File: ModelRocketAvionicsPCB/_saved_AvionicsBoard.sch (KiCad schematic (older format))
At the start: 39 parts, among them CON1 microSD_Card, P1 FTSH-105-01-F-DV, P2 USB_OTG, P3 JST-2, SW1 SW_RST, U1 TM4C123GH6PM, U2 AT25SF161-16Mb_SPI_FLASH, Y1 16Mhz, Y2 32.768kHz

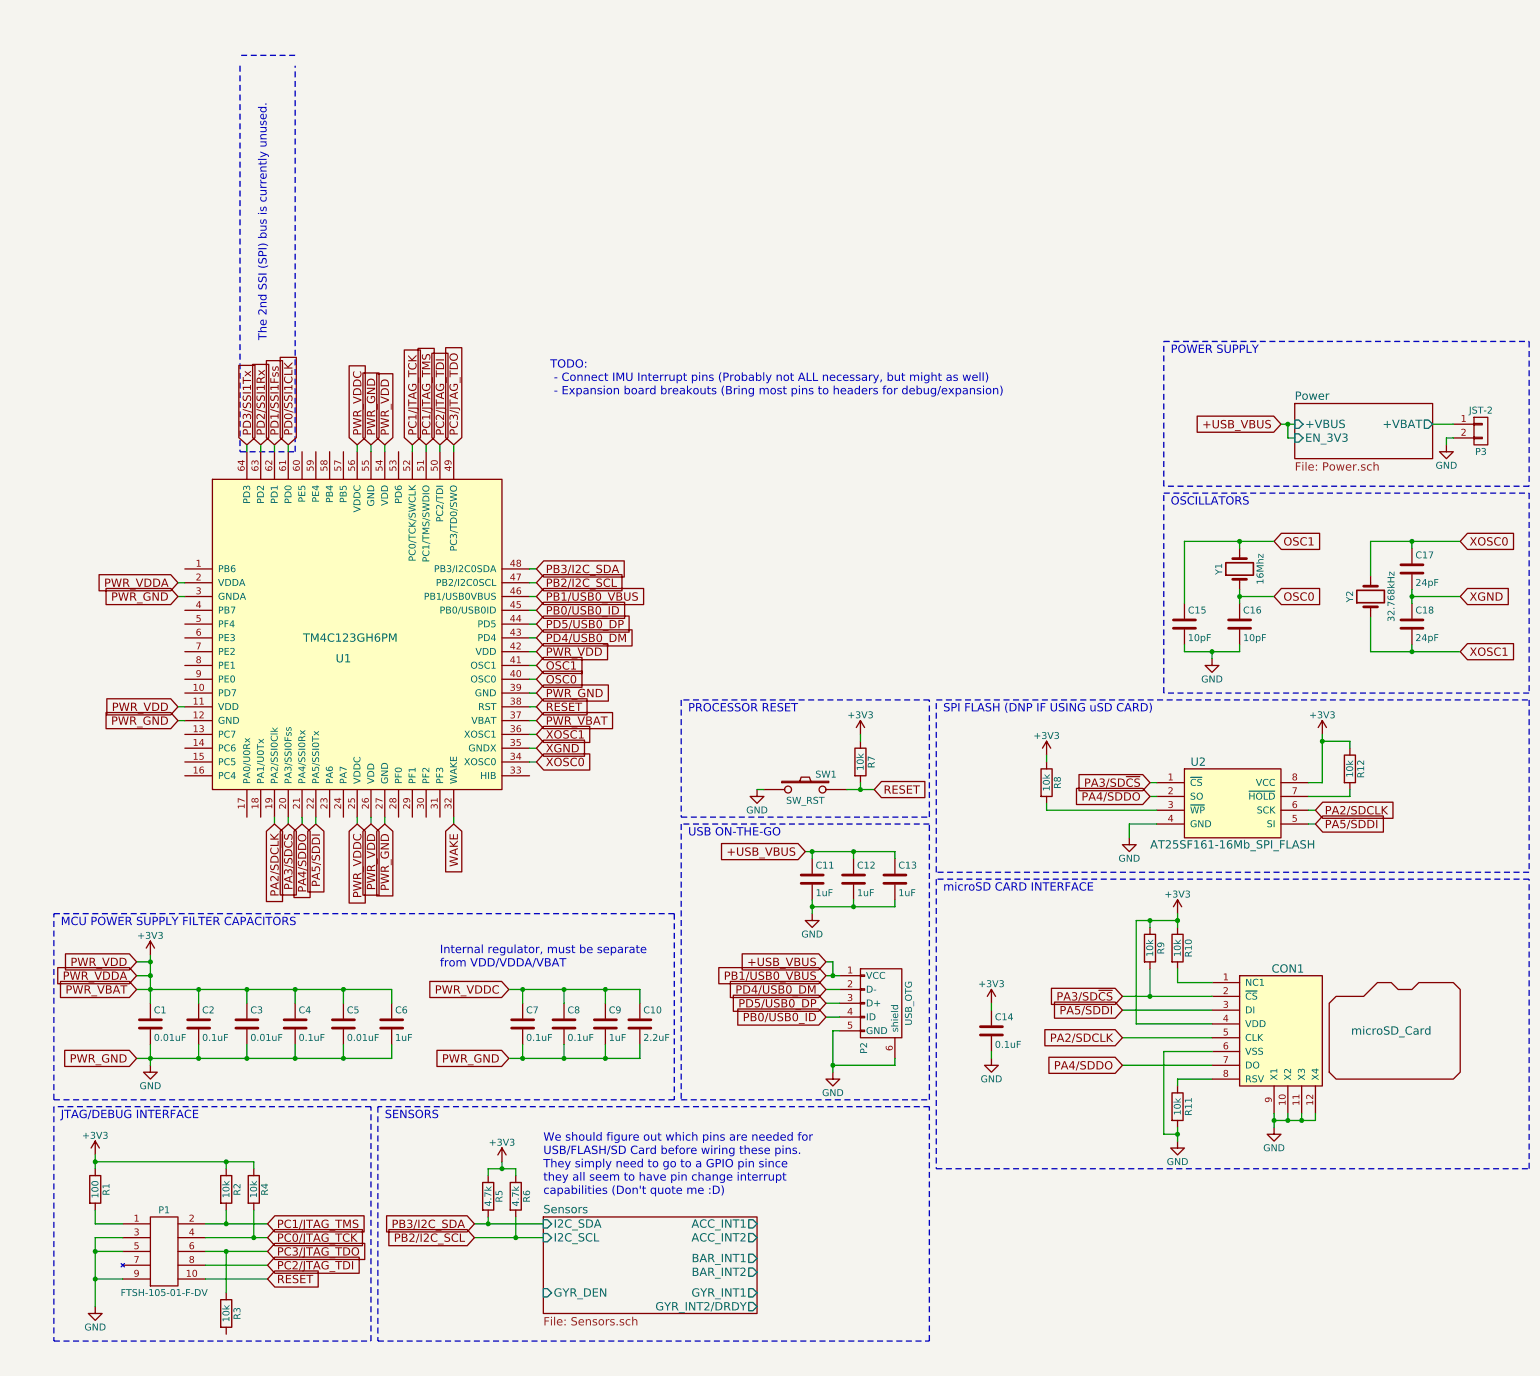
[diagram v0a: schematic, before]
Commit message: Completed Preliminary Layout
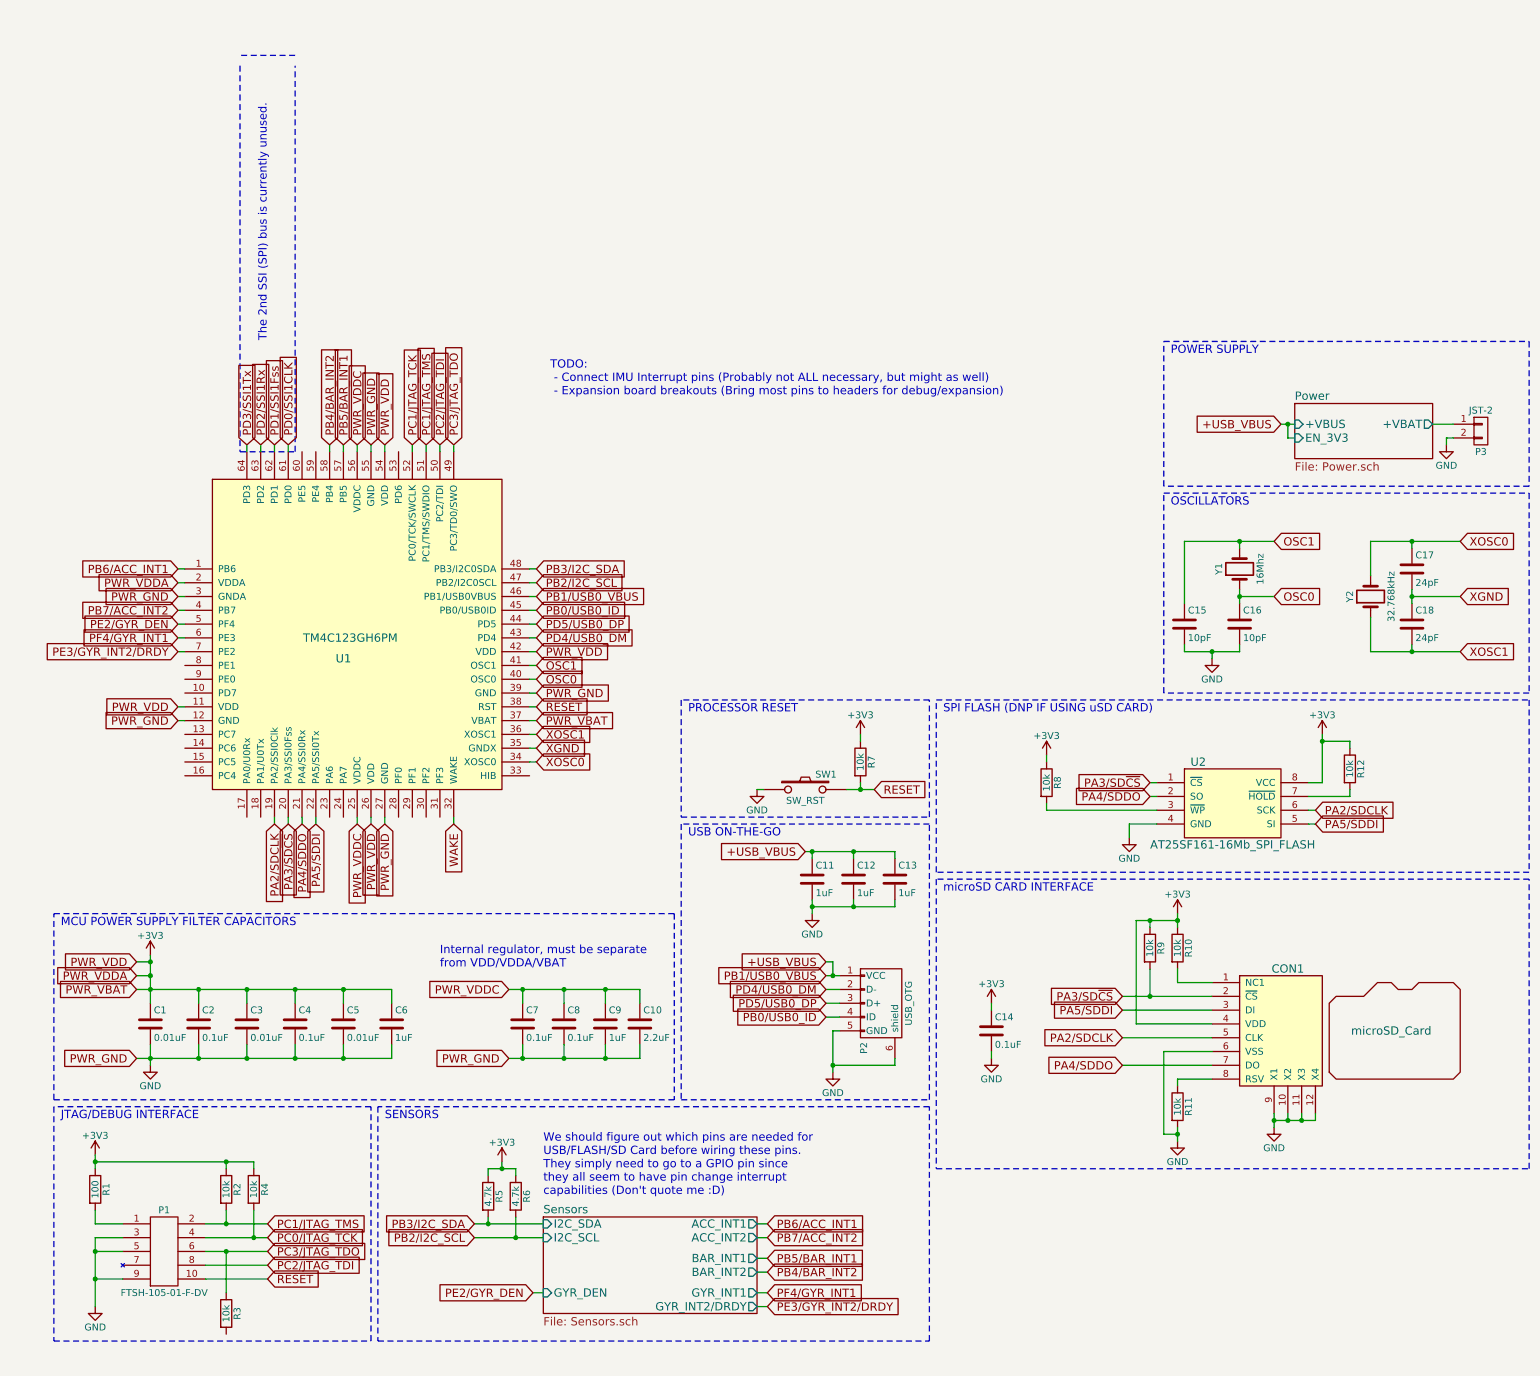
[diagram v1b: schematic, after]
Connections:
- net PB6/ACC_INT1: now reaches U1.1 (PB6)
- net PB7/ACC_INT2: now reaches U1.4 (PB7)
- net PE2/GYR_DEN: now reaches U1.5 (PF4)
- net PB5/BAR_INT1: now reaches U1.57 (PB5)
- net PB4/BAR_INT2: now reaches U1.58 (PB4)
- net PF4/GYR_INT1: now reaches U1.6 (PE3)
- net PE3/GYR_INT2/DRDY: now reaches U1.7 (PE2)
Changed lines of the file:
@@
 Wire Wire Line
 	2200 1300 2200 1250
+Text GLabel 1400 2450 0    60   Input ~ 0
+PB7/ACC_INT2
+Wire Wire Line
+	1450 2450 1400 2450
+Text GLabel 1400 2150 0    60   Input ~ 0
+PB6/ACC_INT1
+Text GLabel 1400 2650 0    60   Input ~ 0
+PF4/GYR_INT1
+Text GLabel 1400 2750 0    60   Input ~ 0
+PE3/GYR_INT2/DRDY
+Text GLabel 1400 2550 0    60   Input ~ 0
+PE2/GYR_DEN
+Text GLabel 2600 1250 1    60   Input ~ 0
+PB5/BAR_INT1
+Text GLabel 2500 1250 1    60   Input ~ 0
+PB4/BAR_INT2
+Wire Wire Line
+	2600 1300 2600 1250
+Wire Wire Line
+	2500 1300 2500 1250
+Text GLabel 3975 7400 0    60   Input ~ 0
+PE2/GYR_DEN
+Text GLabel 5675 7500 2    60   Input ~ 0
+PE3/GYR_INT2/DRDY
+Text GLabel 5675 7400 2    60   Input ~ 0
+PF4/GYR_INT1
+Text GLabel 5675 7000 2    60   Input ~ 0
+PB7/ACC_INT2
+Text GLabel 5675 6900 2    60   Input ~ 0
+PB6/ACC_INT1
+Text GLabel 5675 7250 2    60   Input ~ 0
+PB4/BAR_INT2
+Text GLabel 5675 7150 2    60   Input ~ 0
+PB5/BAR_INT1
+Wire Wire Line
+	5600 7500 5675 7500
+Wire Wire Line
+	5675 7400 5600 7400
+Wire Wire Line
+	5675 7250 5600 7250
+Wire Wire Line
+	5600 7150 5675 7150
+Wire Wire Line
+	5675 7000 5600 7000
+Wire Wire Line
+	5600 6900 5675 6900
+Wire Wire Line
+	1400 2150 1450 2150
+Wire Wire Line
+	1400 2550 1450 2550
+Wire Wire Line
+	1450 2650 1400 2650
+Wire Wire Line
+	1400 2750 1450 2750
+Wire Wire Line
+	3975 7400 4050 7400
 $EndSCHEMATC

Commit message: Partially Complete Updated Avionics Layout
Final Pinout and Silk Screen still needs to be completed.
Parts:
- added D3: Led_Small, SFUSAT-Res:R_0603, symbol Led_Small
- added R15: 330, SFUSAT-Res:R_0402, symbol R
- added U8, U9: CONNHeaderFemale16, Avionics:16x1_Female_Header, symbol CONNHeaderFemale16
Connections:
- net PC1/JTAG_TCK is gone; now on net PC0/JTAG_TCK: U1.52 (PC0/TCK/SWCLK)
- net GND: now also R3.2, D3.1 (K)
- net PE1/IND_LED: now reaches U1.8 (PE1)
- net PE1/IND_LED: now also R15.2
- net Power/+VBAT renamed Power Switch/+VBAT
- new net: D3.2 (A), R15.1
- new net +VBAT: U8.16
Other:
- note added: "Indicator LED"
- note added: "Left Side Female Header\n"
- note added: "Power Switch - Slide Switch and P-MOSFET"
- note added: "Right Side Female Header"
- moved on the sheet: P3

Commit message: CDR Ready Board
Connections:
- net PB4/BAR_INT2 is gone; now on net PB4: U1.58 (PB4)
- net PB5/BAR_INT1 is gone; now on net PB5: U1.57 (PB5)
- net +3V3: now also U8.3, U8.4, U9.16
- net +VBAT: now also U8.1, U8.2; no longer U8.16
- net GND: now also U8.16, U9.1, U9.2
- net PB2/I2C_SCL: now also U9.3
- net PB3/I2C_SDA: now also U9.4
- net PD0/SSI1CLK: now also U9.12
- net PD1/SSI1Fss: now also U9.13
- net PD2/SSI1Rx: now also U9.14
- net PD3/SSI1Tx: now also U9.15
- net RESET: now also U9.6
- net WAKE: now also U8.5
- net PD7: now reaches U1.10 (PD7)
- net PD7: now also U8.14
- net PC7: now reaches U1.13 (PC7)
- net PC7: now also U8.13
- net PC6: now reaches U1.14 (PC6)
- net PC6: now also U8.12
- net PC5: now reaches U1.15 (PC5)
- net PC5: now also U8.11
- net PC4: now reaches U1.16 (PC4)
- net PC4: now also U8.10
- net PA0/U0Rx: now reaches U1.17 (PA0/U0Rx)
- net PA0/U0Rx: now also U8.9
- net PA1/U0Tx: now reaches U1.18 (PA1/U0Tx)
- net PA1/U0Tx: now also U8.8
- net PA6: now reaches U1.23 (PA6)
- net PA6: now also U8.7
- net PA7: now reaches U1.24 (PA7)
- net PA7: now also U8.6
- net PF0: now reaches U1.28 (PF0)
- net PF1: now reaches U1.29 (PF1)
- net PF2/BAR_INT1: now reaches U1.30 (PF2)
- net PF3/BAR_INT2: now reaches U1.31 (PF3)
- net HIB: now reaches U1.33 (HIB)
- net HIB: now also U9.7
- net PD6: now reaches U1.53 (PD6)
- net PD6: now also U9.5
- net PE4: now reaches U1.59 (PE4)
- net PE4: now also U9.10
- net PE5: now reaches U1.60 (PE5)
- net PE5: now also U9.11
- net PE0: now reaches U1.9 (PE0)
- net PE0: now also U8.15
- net PB5: now reaches U9.8
- net PB4: now reaches U9.9
- net PB6/ACC_INT1 renamed PB6/GYR_INT2/DRDY
- net PB7/ACC_INT2 renamed PB7/GYR_INT1
- net PD4/USB0_DM renamed USB0_D-
- net PD5/USB0_DP renamed USB0_D+
- net PE2/GYR_DEN renamed PF4/GYR_DEN
- net PE3/GYR_INT2/DRDY renamed PE2/ACC_INT2
- net PF4/GYR_INT1 renamed PE3/ACC_INT1
